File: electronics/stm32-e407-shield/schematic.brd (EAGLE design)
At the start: 100 x 80 mm, 36 parts, among them IC1 MAX3468CPA, IC2 LM340H-12, IC3 LM340H-12

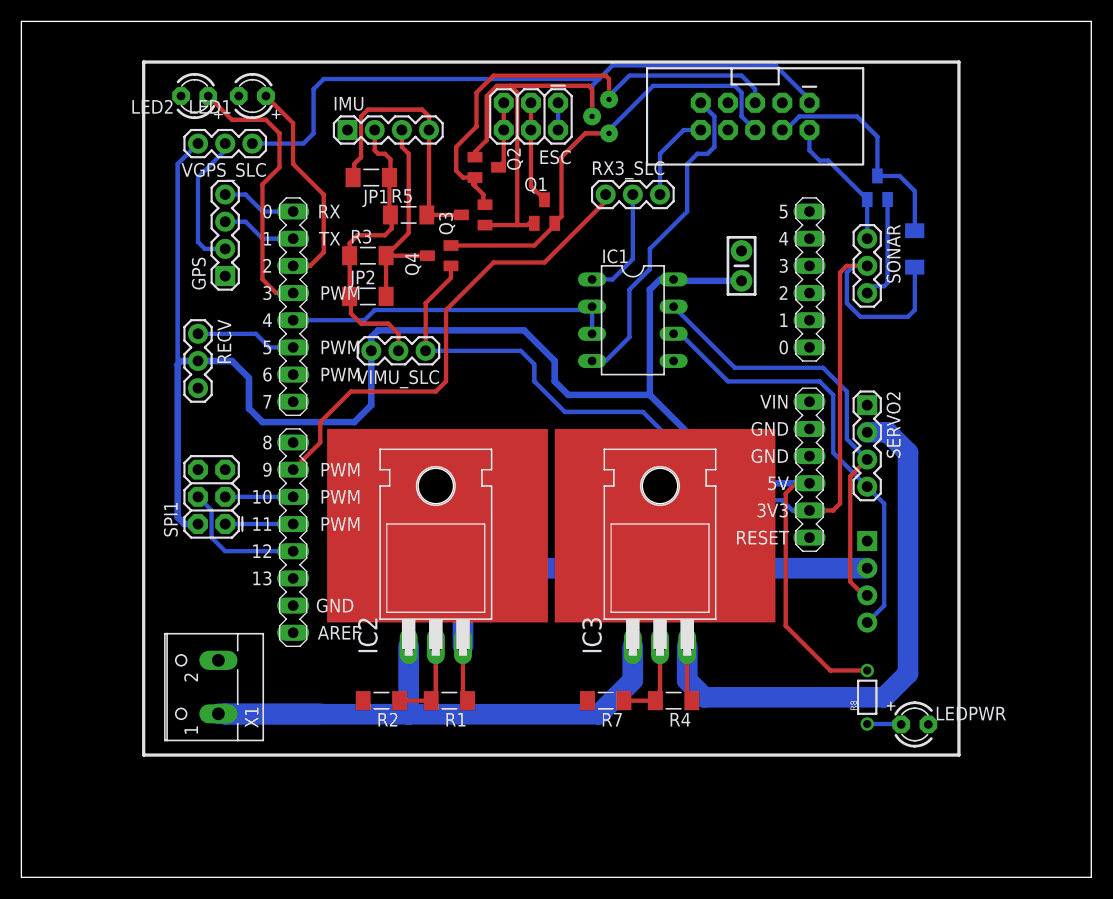
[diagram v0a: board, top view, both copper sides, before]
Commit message: Alterações no Shield para ARM e biblioteca padrão.
O conversor lógico foi modelado no Eagle e adicionado à recem criada
biblioteca provant_custom.lbr. Ele foi então usado para substituir
o coversor lógico hard-core que havia sido previamente projetado.

Planos para remover o IMU_SLC - ele agora influencia a tensão do
barramento do ESC, o que não é desejado.

	new file:   .gitignore
	new file:   lib/.gitignore
	new file:   lib/provant_custom.lbr
	modified:   stm32-e407-shield/schematic.brd
	modified:   stm32-e407-shield/schematic.sch
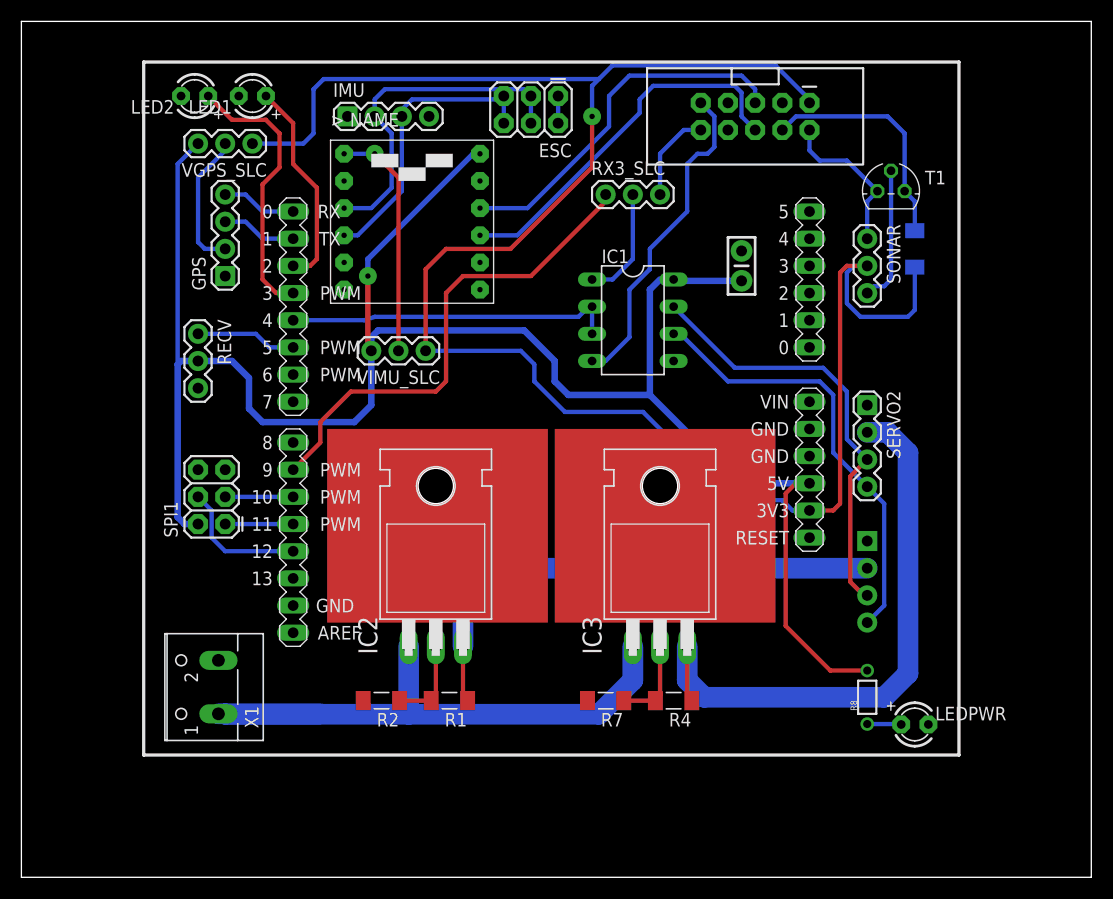
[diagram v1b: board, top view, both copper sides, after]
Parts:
- removed JP1, JP2: 0, adafruit:M1406
- removed Q1, Q2, Q3, Q4, Q5: (no value), adafruit:SOT23
- removed R3, R5: 4k7, adafruit:M1406
- added T1: 2N3565, transistor:TO92
- added U$1: JYMCU_LOGIC_LEVEL_CONVERTER, provant_custom:JYMCU_LOGIC_LEVEL_SHIFTER_DIP
- moved IMU 1.27 mm to (30.5, 71.1)
- moved ESC 0.64 mm to (50.2, 73.0)
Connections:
- removed net N$2: ESC.3, ESC.4, Q1.3
- removed net N$4: ESC.5, ESC.6, Q2.3
- removed net N$5: IMU.3, JP2.2, Q4.3, R3.2
- new net N$12: ESC.5, ESC.6, IMU.3, U$1.BL
- net 3.3V: no longer Q1.1, Q2.1, Q3.1, Q4.1
- net 5V: now also U$1.5V
- net GND: now also T1.3, U$1.GND1, U$1.GND2; no longer Q5.2
- net N$1: now also U$1.3V3, VIMU_SLC.2; no longer IMU.4, JP1.2, Q3.3, R5.2
- net N$6: now also T1.2; no longer Q5.1
- net N$7: now also ESC.3, ESC.4, U$1.AL; no longer JP1.1, JP2.1, R3.1, R5.1, VIMU_SLC.2
- net PB8_I2C1_SCL: now also U$1.AH; no longer Q2.2, Q3.2
- net PB9_I2C1_SDA: now also U$1.BH; no longer Q1.2, Q4.2
- net PC7_USART6_RX: now also T1.1; no longer Q5.3
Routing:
- net N$12: track 0.00 -> 28.0 mm
- net 5V: track 158.6 -> 181.9 mm, vias 0 -> 1
- net N$5: track 20.6 -> 0.00 mm
- net 3.3V: track 195.6 -> 181.5 mm
- net PB8_I2C1_SCL: track 46.0 -> 35.0 mm, vias 1 -> 0
- net N$2: track 9.59 -> 0.00 mm
- net N$4: track 6.23 -> 0.00 mm
- net PB9_I2C1_SDA: track 41.2 -> 35.3 mm, vias 1 -> 0
- net N$7: track 28.3 -> 31.9 mm
- net N$1: track 25.5 -> 22.2 mm, vias 0 -> 1
- net N$6: track 10.1 -> 12.9 mm
- net GND: track 15.4 -> 17.2 mm
- net PB11_UART3_RX: track 45.3 -> 46.2 mm
- net N$9: track 20.2 -> 19.7 mm

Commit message: Versão dual layer pra fabricação manual.
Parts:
- R1, R4: device adafruit:M1406 -> adafruit:0309V
- R2, R7: device adafruit:M1406 -> adafruit:0204/7
- moved R7 2.03 mm to (53.3, 18.1)
- moved R1 1.59 mm to (40.0, 18.1)
- moved R4 1.59 mm to (61.0, 18.1)
- moved R2 1.42 mm to (34.9, 15.9)
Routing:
- net VSERVO2: track 56.7 -> 52.3 mm
- net BAT_VCC: track 58.5 -> 54.5 mm
- net N$16: track 8.21 -> 5.71 mm
- net N$15: track 8.21 -> 6.03 mm
- net VSERVO1: track 48.7 -> 46.9 mm
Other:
- board text added: "proVANT board.v1"
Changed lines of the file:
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@@
 <layer number="25" name="tNames" color="7" fill="1" visible="yes" active="yes"/>
 <layer number="26" name="bNames" color="7" fill="1" visible="yes" active="yes"/>
-<layer number="27" name="tValues" color="7" fill="1" visible="yes" active="yes"/>
-<layer number="28" name="bValues" color="7" fill="1" visible="yes" active="yes"/>
+<layer number="27" name="tValues" color="7" fill="1" visible="no" active="yes"/>
+<layer number="28" name="bValues" color="7" fill="1" visible="no" active="yes"/>
 <layer number="29" name="tStop" color="7" fill="3" visible="yes" active="yes"/>
 <layer number="30" name="bStop" color="7" fill="6" visible="yes" active="yes"/>
@@
 <rectangle x1="28.575" y1="23.8125" x2="49.2125" y2="41.91" layer="1"/>
 <rectangle x1="49.8475" y1="23.8125" x2="70.485" y2="41.91" layer="1"/>
+<text x="66.3575" y="12.3825" size="1.524" layer="1">proVANT
+board.v1</text>
 </plain>
 <attributes>
@@
 <element name="IC2" library="linear" package="TO220H" value="LM340H-12" x="38.735" y="31.75"/>
 <element name="IC3" library="linear" package="TO220H" value="LM340H-12" x="59.69" y="31.75"/>
-<element name="R1" library="adafruit" package="M1406" value="4k7" x="40.005" y="16.51" rot="R180"/>
-<element name="R2" library="adafruit" package="M1406" value="4k7" x="33.655" y="16.51" rot="R180"/>
-<element name="R4" library="adafruit" package="M1406" value="4k7" x="60.96" y="16.51" rot="R180"/>
-<element name="R7" library="adafruit" package="M1406" value="4k7" x="54.61" y="16.51" rot="R180"/>
+<element name="R1" library="adafruit" package="0309V" value="4k7" x="40.005" y="18.0975" rot="R180"/>
+<element name="R2" library="adafruit" package="0204/7" value="4k7" x="34.925" y="15.875" rot="R180"/>
+<element name="R4" library="adafruit" package="0309V" value="4k7" x="60.96" y="18.0975" rot="R180"/>
+<element name="R7" library="adafruit" package="0204/7" value="4k7" x="53.34" y="18.0975" rot="R180"/>
 <element name="LED1" library="adafruit" package="LED3MM" value="" x="21.59" y="73.025" rot="R180"/>
 <element name="LED2" library="adafruit" package="LED3MM" value="" x="16.1925" y="73.025" rot="R180"/>
@@
 <wire x1="41.275" y1="21.59" x2="41.275" y2="26.035" width="1.9304" layer="16"/>
 <wire x1="41.275" y1="26.035" x2="44.1325" y2="28.8925" width="1.9304" layer="16"/>
-<wire x1="41.275" y1="21.59" x2="41.275" y2="16.94" width="0.4064" layer="1"/>
-<wire x1="41.275" y1="16.94" x2="41.705" y2="16.51" width="0.4064" layer="1"/>
+<wire x1="41.275" y1="18.0975" x2="41.275" y2="21.59" width="0.4064" layer="16"/>
 </signal>
 <signal name="VSERVO2">
@@
 <contactref element="IC3" pad="3"/>
 <contactref element="R4" pad="1"/>
-<wire x1="62.23" y1="16.94" x2="62.66" y2="16.51" width="0.4064" layer="1"/>
 <wire x1="80.645" y1="16.8275" x2="82.8675" y2="19.05" width="1.9304" layer="16"/>
 <wire x1="82.8675" y1="19.05" x2="82.8675" y2="39.6875" width="1.9304" layer="16"/>
 <wire x1="82.8675" y1="39.6875" x2="80.9625" y2="41.5925" width="1.9304" layer="16"/>
 <wire x1="80.9625" y1="41.5925" x2="79.0575" y2="41.5925" width="1.9304" layer="16"/>
-<wire x1="80.645" y1="16.8275" x2="63.8175" y2="16.8275" width="1.9304" layer="16"/>
-<wire x1="63.8175" y1="16.8275" x2="62.23" y2="18.415" width="1.9304" layer="16"/>
-<wire x1="62.23" y1="18.415" x2="62.23" y2="21.59" width="1.9304" layer="16"/>
-<wire x1="62.66" y1="16.51" x2="62.23" y2="16.51" width="0.4064" layer="1"/>
-<wire x1="62.23" y1="16.51" x2="62.23" y2="21.59" width="0.4064" layer="1"/>
+<wire x1="80.645" y1="16.8275" x2="72.0725" y2="16.8275" width="1.9304" layer="16"/>
+<wire x1="72.0725" y1="16.8275" x2="67.31" y2="21.59" width="1.9304" layer="16"/>
+<wire x1="67.31" y1="21.59" x2="62.23" y2="21.59" width="1.9304" layer="16"/>
+<wire x1="62.23" y1="18.0975" x2="62.23" y2="21.59" width="0.4064" layer="16"/>
 </signal>
 <signal name="BAT_VCC">
@@
 <contactref element="IC3" pad="1"/>
 <wire x1="18.415" y1="15.28" x2="19.05" y2="15.28" width="1.9304" layer="16"/>
-<wire x1="19.05" y1="15.28" x2="27.98" y2="15.28" width="1.9304" layer="16"/>
 <wire x1="19.09" y1="15.24" x2="19.05" y2="15.28" width="1.9304" layer="16"/>
-<wire x1="19.09" y1="15.24" x2="36.195" y2="15.24" width="1.9304" layer="16"/>
-<wire x1="36.195" y1="15.24" x2="53.975" y2="15.24" width="1.9304" layer="16"/>
-<wire x1="53.975" y1="15.24" x2="57.15" y2="18.415" width="1.9304" layer="16"/>
-<wire x1="57.15" y1="18.415" x2="57.15" y2="21.59" width="1.9304" layer="16"/>
-<wire x1="36.195" y1="21.59" x2="36.195" y2="15.24" width="1.9304" layer="16"/>
+<wire x1="36.195" y1="21.59" x2="36.195" y2="14.9225" width="1.9304" layer="16"/>
+<wire x1="36.195" y1="14.9225" x2="37.7825" y2="13.335" width="1.9304" layer="16"/>
+<wire x1="37.7825" y1="13.335" x2="42.2275" y2="13.335" width="1.9304" layer="16"/>
+<wire x1="42.2275" y1="13.335" x2="44.1325" y2="15.24" width="1.9304" layer="16"/>
+<wire x1="44.1325" y1="15.24" x2="44.1325" y2="19.3675" width="1.9304" layer="16"/>
+<wire x1="44.1325" y1="19.3675" x2="46.355" y2="21.59" width="1.9304" layer="16"/>
+<wire x1="46.355" y1="21.59" x2="57.15" y2="21.59" width="1.9304" layer="16"/>
+<wire x1="19.09" y1="15.24" x2="24.4475" y2="15.24" width="1.9304" layer="16"/>
+<wire x1="24.4475" y1="15.24" x2="30.7975" y2="21.59" width="1.9304" layer="16"/>
+<wire x1="30.7975" y1="21.59" x2="36.195" y2="21.59" width="1.9304" layer="16"/>
 </signal>
 <signal name="N$15">
@@
 <contactref element="R7" pad="1"/>
 <contactref element="IC3" pad="2"/>
-<wire x1="56.31" y1="16.51" x2="59.26" y2="16.51" width="0.4064" layer="1"/>
-<wire x1="59.69" y1="21.59" x2="59.69" y2="16.94" width="0.4064" layer="1"/>
-<wire x1="59.69" y1="16.94" x2="59.26" y2="16.51" width="0.4064" layer="1"/>
+<wire x1="59.69" y1="18.0975" x2="59.69" y2="21.59" width="0.4064" layer="16"/>
+<wire x1="57.15" y1="18.0975" x2="59.69" y2="18.0975" width="0.4064" layer="16"/>
 </signal>
 <signal name="N$16">
@@
 <contactref element="R2" pad="1"/>
 <contactref element="IC2" pad="2"/>
-<wire x1="38.735" y1="21.59" x2="38.735" y2="16.94" width="0.4064" layer="1"/>
-<wire x1="38.735" y1="16.94" x2="38.305" y2="16.51" width="0.4064" layer="1"/>
-<wire x1="35.355" y1="16.51" x2="38.305" y2="16.51" width="0.4064" layer="1"/>
+<wire x1="38.735" y1="18.0975" x2="38.735" y2="21.59" width="0.4064" layer="16"/>
+<wire x1="38.735" y1="15.875" x2="38.735" y2="18.0975" width="0.4064" layer="16"/>
 </signal>
 <signal name="N$8">
@@
 </board>
 </drawing>
+<compatibility>
+<note version="6.3" minversion="6.2.2" severity="warning">
+Since Version 6.2.2 text objects can contain more than one line,
+which will not be processed correctly with this version.
+</note>
+</compatibility>
 </eagle>

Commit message: Pequenas correções depois da primeira tentativa de fabricação.
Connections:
- net N$1: now also IMU.4
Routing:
- net N$1: track 22.2 -> 28.7 mm
- net 3.3V: track 181.5 -> 182.8 mm
- net N$7: track 31.9 -> 32.7 mm
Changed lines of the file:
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@@
 <via x="53.34" y="71.12" extent="1-16" drill="0.5" diameter="1.6764" shape="octagon"/>
 <wire x1="53.34" y1="71.12" x2="53.34" y2="73.9775" width="0.4064" layer="16"/>
-<wire x1="53.34" y1="73.9775" x2="53.975" y2="74.6125" width="0.4064" layer="16"/>
-<wire x1="53.975" y1="74.6125" x2="55.245" y2="75.8825" width="0.4064" layer="16"/>
+<wire x1="53.34" y1="73.9775" x2="54.9275" y2="75.565" width="0.4064" layer="16"/>
+<wire x1="55.08625" y1="75.72375" x2="55.245" y2="75.8825" width="0.4064" layer="16"/>
 <wire x1="37.7825" y1="49.2125" x2="37.7825" y2="56.8325" width="0.4064" layer="1"/>
 <wire x1="55.245" y1="75.8825" x2="70.485" y2="75.8825" width="0.4064" layer="16"/>
@@
 <wire x1="77.1525" y1="57.15" x2="79.0575" y2="57.15" width="0.4064" layer="1"/>
 <wire x1="72.0725" y1="34.29" x2="73.66" y2="34.29" width="0.4064" layer="16"/>
-<wire x1="28.2575" y1="74.6125" x2="53.975" y2="74.6125" width="0.4064" layer="16"/>
 <wire x1="21.59" y1="68.58" x2="26.3525" y2="68.58" width="0.4064" layer="16"/>
 <wire x1="26.3525" y1="68.58" x2="27.305" y2="69.5325" width="0.4064" layer="16"/>
 <wire x1="27.305" y1="69.5325" x2="27.305" y2="73.66" width="0.4064" layer="16"/>
-<wire x1="27.305" y1="73.66" x2="28.2575" y2="74.6125" width="0.4064" layer="16"/>
 <wire x1="37.7825" y1="56.8325" x2="39.6875" y2="58.7375" width="0.4064" layer="1"/>
 <wire x1="39.6875" y1="58.7375" x2="45.72" y2="58.7375" width="0.4064" layer="1"/>
 <wire x1="45.72" y1="58.7375" x2="53.34" y2="66.3575" width="0.4064" layer="1"/>
 <wire x1="53.34" y1="66.3575" x2="53.34" y2="71.12" width="0.4064" layer="1"/>
+<wire x1="27.305" y1="73.66" x2="29.21" y2="75.565" width="0.4064" layer="16"/>
+<wire x1="29.21" y1="75.565" x2="54.9275" y2="75.565" width="0.4064" layer="16"/>
+<wire x1="54.9275" y1="75.565" x2="55.08625" y2="75.72375" width="0.4064" layer="16"/>
 </signal>
 <signal name="UART3_RX">
@@
 <contactref element="IMU" pad="2"/>
 <wire x1="33.02" y1="71.12" x2="33.02" y2="72.7075" width="0.4064" layer="16"/>
-<wire x1="33.02" y1="72.7075" x2="33.9725" y2="73.66" width="0.4064" layer="16"/>
-<wire x1="33.9725" y1="73.66" x2="46.99" y2="73.66" width="0.4064" layer="16"/>
-<wire x1="46.99" y1="73.66" x2="47.625" y2="73.025" width="0.4064" layer="16"/>
+<wire x1="33.02" y1="72.7075" x2="33.655" y2="73.3425" width="0.4064" layer="16"/>
+<wire x1="33.655" y1="73.3425" x2="33.9725" y2="73.66" width="0.4064" layer="16"/>
 <wire x1="30.1625" y1="62.5475" x2="32.7025" y2="62.5475" width="0.4064" layer="16"/>
 <wire x1="32.7025" y1="62.5475" x2="34.6075" y2="64.4525" width="0.4064" layer="16"/>
 <wire x1="34.6075" y1="64.4525" x2="34.6075" y2="69.5325" width="0.4064" layer="16"/>
 <wire x1="34.6075" y1="69.5325" x2="33.02" y2="71.12" width="0.4064" layer="16"/>
+<wire x1="47.625" y1="73.025" x2="46.0375" y2="74.6125" width="0.4064" layer="16"/>
+<wire x1="46.0375" y1="74.6125" x2="34.925" y2="74.6125" width="0.4064" layer="16"/>
+<wire x1="34.925" y1="74.6125" x2="33.9725" y2="73.66" width="0.4064" layer="16"/>
 </signal>
 <signal name="N$1">
@@
 <via x="33.02" y="67.6275" extent="1-16" drill="0.5" diameter="1.6764" shape="octagon"/>
 <wire x1="33.02" y1="67.6275" x2="30.1625" y2="67.6275" width="0.4064" layer="16"/>
+<contactref element="IMU" pad="4"/>
+<wire x1="33.02" y1="67.6275" x2="34.6075" y2="67.6275" width="0.4064" layer="1"/>
+<wire x1="34.6075" y1="67.6275" x2="38.1" y2="71.12" width="0.4064" layer="1"/>
 </signal>
 </signals>
